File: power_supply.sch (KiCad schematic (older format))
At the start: 1 part

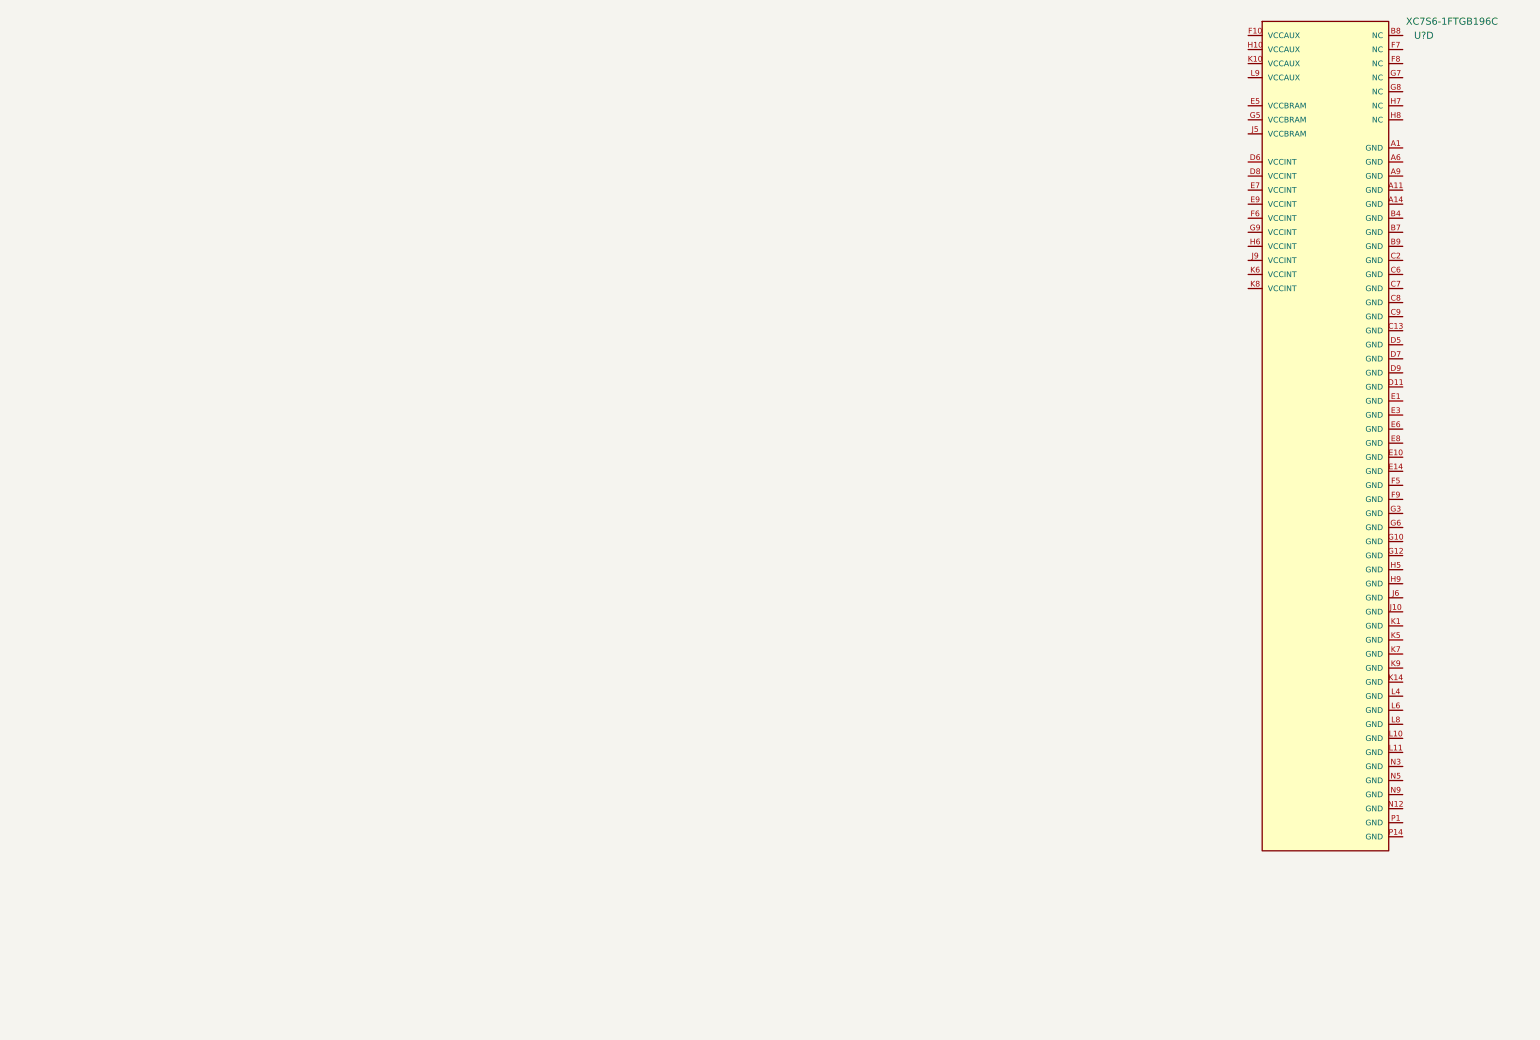
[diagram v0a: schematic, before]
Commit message: FPGA supply notes
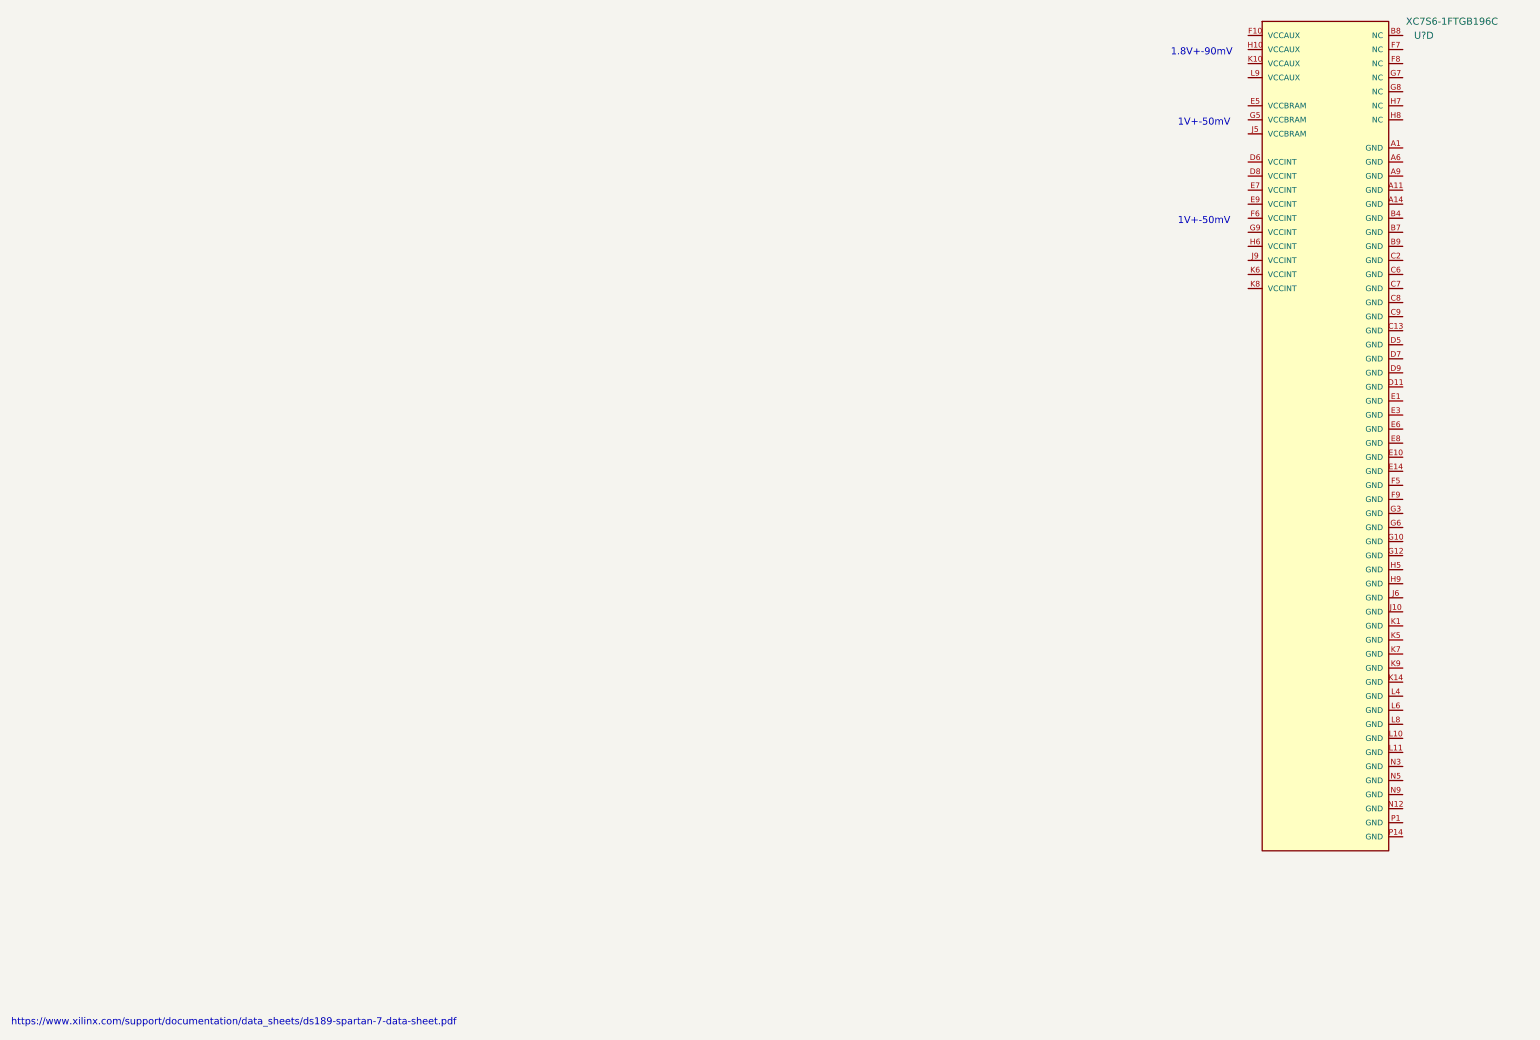
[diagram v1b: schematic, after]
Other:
- note added: "1.8V+-90mV"
- note added: "1V+-50mV"
- note added: "https://www.xilinx.com/support/documentation/data_sheets/ds189-spartan-7-data-sheet.pdf"
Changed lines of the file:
@@
 $Descr A4 11693 8268
 encoding utf-8
-Sheet 1 1
+Sheet 13 14
 Title "Open HF SDR FPGA Sheet"
 Date "2021-01-16"
@@
 	1    0    0    -1
 $EndComp
+Text Notes 8900 2000 0    50   ~ 0
+1V+-50mV
+Text Notes 600  7700 0    50   ~ 0
+https://www.xilinx.com/support/documentation/data_sheets/ds189-spartan-7-data-sheet.pdf
+Text Notes 8850 800  0    50   ~ 0
+1.8V+-90mV
+Text Notes 8900 1300 0    50   ~ 0
+1V+-50mV
 $EndSCHEMATC

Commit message: PSU init
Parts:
- added C? (x4): 4u7, symbol Device:C
- added C? (x2): 100n, symbol Device:C
- added L?: 47u, symbol Device:L
- added L?: 68u, symbol Device:L
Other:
- note added: "https://datasheet.lcsc.com/szlcsc/Silergy-Corp-SY8029AIC_C207636.pdf"
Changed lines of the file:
@@
 Text Notes 8900 1300 0    50   ~ 0
 1V+-50mV
+Text Notes 2550 5250 0    50   ~ 0
+https://datasheet.lcsc.com/szlcsc/Silergy-Corp-SY8029AIC_C207636.pdf
+$Comp
+L Device:L L?
+U 1 1 600CB20B
+P 5150 2000
+F 0 "L?" V 4878 2000 50  0000 C CNN
+F 1 "47u" V 4969 2000 50  0000 C CNN
+F 2 "" H 5150 2000 50  0001 C CNN
+F 3 "~" H 5150 2000 50  0001 C CNN
+F 4 "93-01-06" V 5060 2000 50  0000 C CNN "Lomex"
+	1    5150 2000
+	0    1    1    0
+$EndComp
+$Comp
+L Device:C C?
+U 1 1 600CC1A7
+P 5450 2200
+F 0 "C?" H 5565 2291 50  0000 L CNN
+F 1 "4u7" H 5565 2200 50  0000 L CNN
+F 2 "" H 5488 2050 50  0001 C CNN
+F 3 "~" H 5450 2200 50  0001 C CNN
+F 4 "82-06-22" H 5565 2109 50  0000 L CNN "Lomex"
+	1    5450 2200
+	1    0    0    -1
+$EndComp
+$Comp
+L Device:C C?
+U 1 1 600CC714
+P 6100 2200
+F 0 "C?" H 6215 2291 50  0000 L CNN
+F 1 "4u7" H 6215 2200 50  0000 L CNN
+F 2 "" H 6138 2050 50  0001 C CNN
+F 3 "~" H 6100 2200 50  0001 C CNN
+F 4 "82-06-22" H 6215 2109 50  0000 L CNN "Lomex"
+	1    6100 2200
+	1    0    0    -1
+$EndComp
+$Comp
+L Device:C C?
+U 1 1 600CD1F2
+P 6750 2200
+F 0 "C?" H 6865 2246 50  0000 L CNN
+F 1 "100n" H 6865 2155 50  0000 L CNN
+F 2 "" H 6788 2050 50  0001 C CNN
+F 3 "~" H 6750 2200 50  0001 C CNN
+	1    6750 2200
+	1    0    0    -1
+$EndComp
+$Comp
+L Device:L L?
+U 1 1 600D147C
+P 5150 900
+F 0 "L?" V 4878 900 50  0000 C CNN
+F 1 "68u" V 4969 900 50  0000 C CNN
+F 2 "" H 5150 900 50  0001 C CNN
+F 3 "~" H 5150 900 50  0001 C CNN
+F 4 " 93-03-36" V 5060 900 50  0000 C CNN "Lomex"
+	1    5150 900
+	0    1    1    0
+$EndComp
+$Comp
+L Device:C C?
+U 1 1 600D2019
+P 5450 1150
+F 0 "C?" H 5565 1241 50  0000 L CNN
+F 1 "4u7" H 5565 1150 50  0000 L CNN
+F 2 "" H 5488 1000 50  0001 C CNN
+F 3 "~" H 5450 1150 50  0001 C CNN
+F 4 "82-06-22" H 5565 1059 50  0000 L CNN "Lomex"
+	1    5450 1150
+	1    0    0    -1
+$EndComp
+$Comp
+L Device:C C?
+U 1 1 600D222E
+P 6100 1150
+F 0 "C?" H 6215 1241 50  0000 L CNN
+F 1 "4u7" H 6215 1150 50  0000 L CNN
+F 2 "" H 6138 1000 50  0001 C CNN
+F 3 "~" H 6100 1150 50  0001 C CNN
+F 4 "82-06-22" H 6215 1059 50  0000 L CNN "Lomex"
+	1    6100 1150
+	1    0    0    -1
+$EndComp
+$Comp
+L Device:C C?
+U 1 1 600D2238
+P 6750 1150
+F 0 "C?" H 6865 1196 50  0000 L CNN
+F 1 "100n" H 6865 1105 50  0000 L CNN
+F 2 "" H 6788 1000 50  0001 C CNN
+F 3 "~" H 6750 1150 50  0001 C CNN
+	1    6750 1150
+	1    0    0    -1
+$EndComp
 $EndSCHEMATC

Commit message: Power supplies
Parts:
- removed C? (x2): 4u7, symbol Device:C
- removed C?: 100n, symbol Device:C
- added C? (x24): C, symbol Device:C
- added C? (x4): 4u7, symbol Device:C
- added C? (x2): 100n, symbol Device:C
- added L?: L, symbol Device:L
- added R? (x7): R, symbol Device:R
- added U? (x6): SY8029, Package_TO_SOT_SMD:TSOT-23-8_HandSoldering, symbol sdr:SY8029
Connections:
- net at U?.D6 (VCCINT): now also L?.1, U?.D8 (VCCINT), U?.E5 (VCCBRAM), U?.E7 (VCCINT), U?.E9 (VCCINT), U?.F6 (VCCINT), U?.G5 (VCCBRAM), U?.G9 (VCCINT), U?.H6 (VCCINT), U?.J5 (VCCBRAM), U?.J9 (VCCINT), U?.K6 (VCCINT), U?.K8 (VCCINT), C?.1, C?.1, C?.1, C?.1, C?.1, C?.1, C?.1, C?.1, C?.1, C?.1, C?.1, R?.1
- net at U?.F10 (VCCAUX): now also C?.1, C?.1, C?.1, L?.1, U?.H10 (VCCAUX), U?.K10 (VCCAUX), U?.L9 (VCCAUX), C?.1, C?.1, C?.1, C?.1, C?.1, C?.1, C?.1, C?.1, R?.1
- net at L?.2: now also U?.5 (OUT)
- net at L?.2: now also U?.3 (OUT)
- net GNDD: now reaches C?.2
- net GNDD: now also C?.2, C?.2, C?.2, C?.2, C?.2, C?.2, C?.2, C?.2, R?.2, R?.2, R?.2, R?.2, U?.4 (GND), U?.8 (FB)
- new net: R?.1, R?.2, U?.1 (FB) (x2)
- new net: R?.1, R?.1, R?.2, U?.8 (FB)
- new net: C?.1, C?.1, C?.1, C?.1, C?.1, C?.1, C?.1, C?.1, C?.1, C?.1, C?.1, L?.1, R?.1
- new net: L?.2, U?.3 (OUT)
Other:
- note added: "3.3V"
- note added: "Filter at FPGA"
- note added: "Filter at SMPS"
- note removed: "https://datasheet.lcsc.com/szlcsc/Silergy-Corp-SY8029AIC_C207636.pdf"
- moved on the sheet: C?, L?

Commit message: finish up power supply
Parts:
- removed C? (x2): 4u7, symbol Device:C
- removed C?: 100n, symbol Device:C
- removed C? (x8): C, symbol Device:C
- removed L?: L, symbol Device:L
- removed R? (x2): R, symbol Device:R
- removed U? (x3): SY8029, Package_TO_SOT_SMD:TSOT-23-8_HandSoldering, symbol sdr:SY8029
- added C? (x2): 100n, symbol Device:C
- added C? (x5): 10n, symbol Device:C
- added C? (x2): 47p, symbol Device:C
- added C? (x2): 1n, symbol Device:C
- added C? (x4): 47uF, symbol Device:C
- added C? (x2): 47u, symbol Device:C
- added D? (x2): BAT54CLT1G, symbol Device:D_Schottky
- added D?: ZMM3V3, symbol Device:D_Zener
- added D? (x2): LED, symbol Device:LED
- added J?: Barrel_Jack, symbol Connector:Barrel_Jack
- added J?: _BAT_PROT, symbol Connector:Conn_01x02_Male
- added L?: 6.8u, symbol Device:L
- added L?: 330u, symbol Device:L
- added R? (x4): 10k, symbol Device:R
- added R?: 3.24k, symbol Device:R
- added R?: 1.7k, symbol Device:R
- added R?: 0, symbol Device:R
- added R?: 8k, symbol Device:R
- added R? (x2): 1k, symbol Device:R
- added R?: 470, symbol Device:R
- added U? (x2): TPS54331, symbol sdr:TPS54331
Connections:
- net labels added: +3V3, +5VA, GNDA, PWR_EN, VIN
- wire segments 85 -> 130
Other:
- note added: "10mV ripple with 0.1 ohm ESR per cap"
- note added: "40mVpp ripple with 0.1 ohm ESR per cap"
- note added: "Battery protection"
- note added: "Farnell 2725244"
- note added: "If the jumper is off, and VIN goes below 11.25V, PWR_EN \nwill go below 1.25V, switching off the power.\nThis avoids deep cycling lead acid batteries"
- note added: "Input decoupling\n"
- note added: "Lomex: 55-01-84"
- note added: "Power requirements\n1.8V 1A FPGA\n1V 1A FPGA\n3V3 1.5A FPGA + 1.2A for 1V and 1.8V buck inputs\n5V5 0.1A receiver"
- note removed: "3.3V"
- moved on the sheet: U?D

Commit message: update buck converter diodes
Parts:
- D? (x2): value BAT54CLT1G -> SS34
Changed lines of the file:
@@
 P 6050 3700
 F 0 "D?" V 6150 3550 50  0000 L CNN
-F 1 "BAT54CLT1G" V 6250 3450 50  0000 L CNN
+F 1 "SS34" V 6250 3450 50  0000 L CNN
 F 2 "" H 6050 3700 50  0001 C CNN
 F 3 "~" H 6050 3700 50  0001 C CNN
@@
 P 6000 5450
 F 0 "D?" V 6100 5300 50  0000 L CNN
-F 1 "BAT54CLT1G" V 6200 5200 50  0000 L CNN
+F 1 "SS34" V 6200 5200 50  0000 L CNN
 F 2 "" H 6000 5450 50  0001 C CNN
 F 3 "~" H 6000 5450 50  0001 C CNN

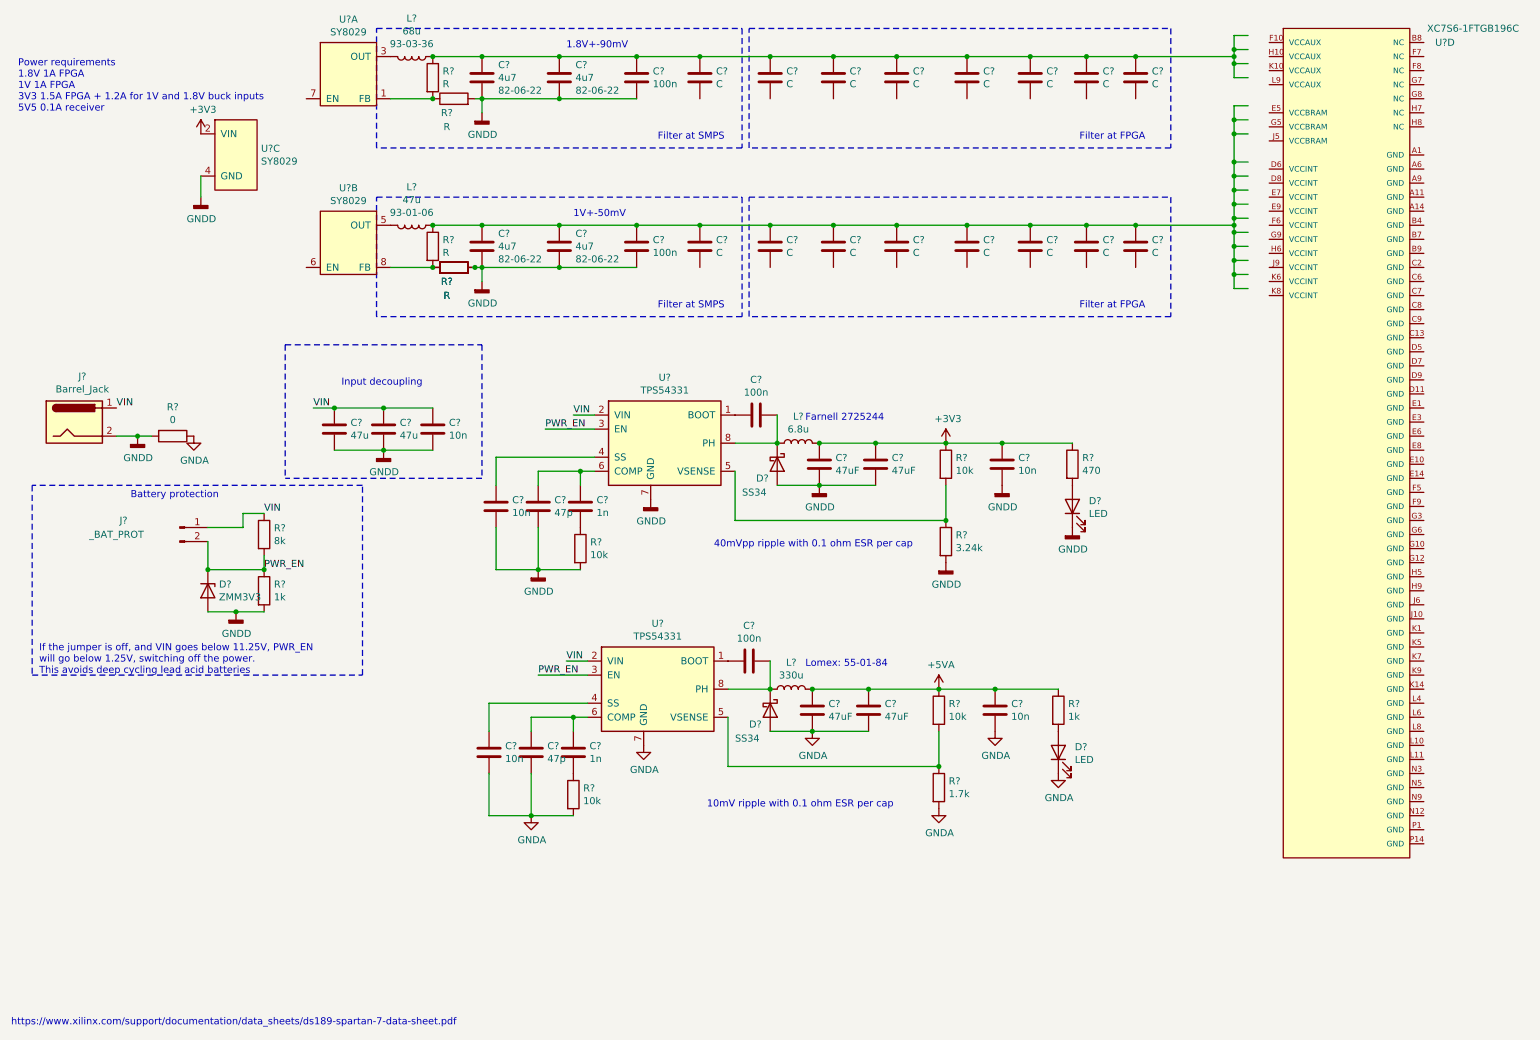
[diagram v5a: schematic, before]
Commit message: add power on sequencing for fpga
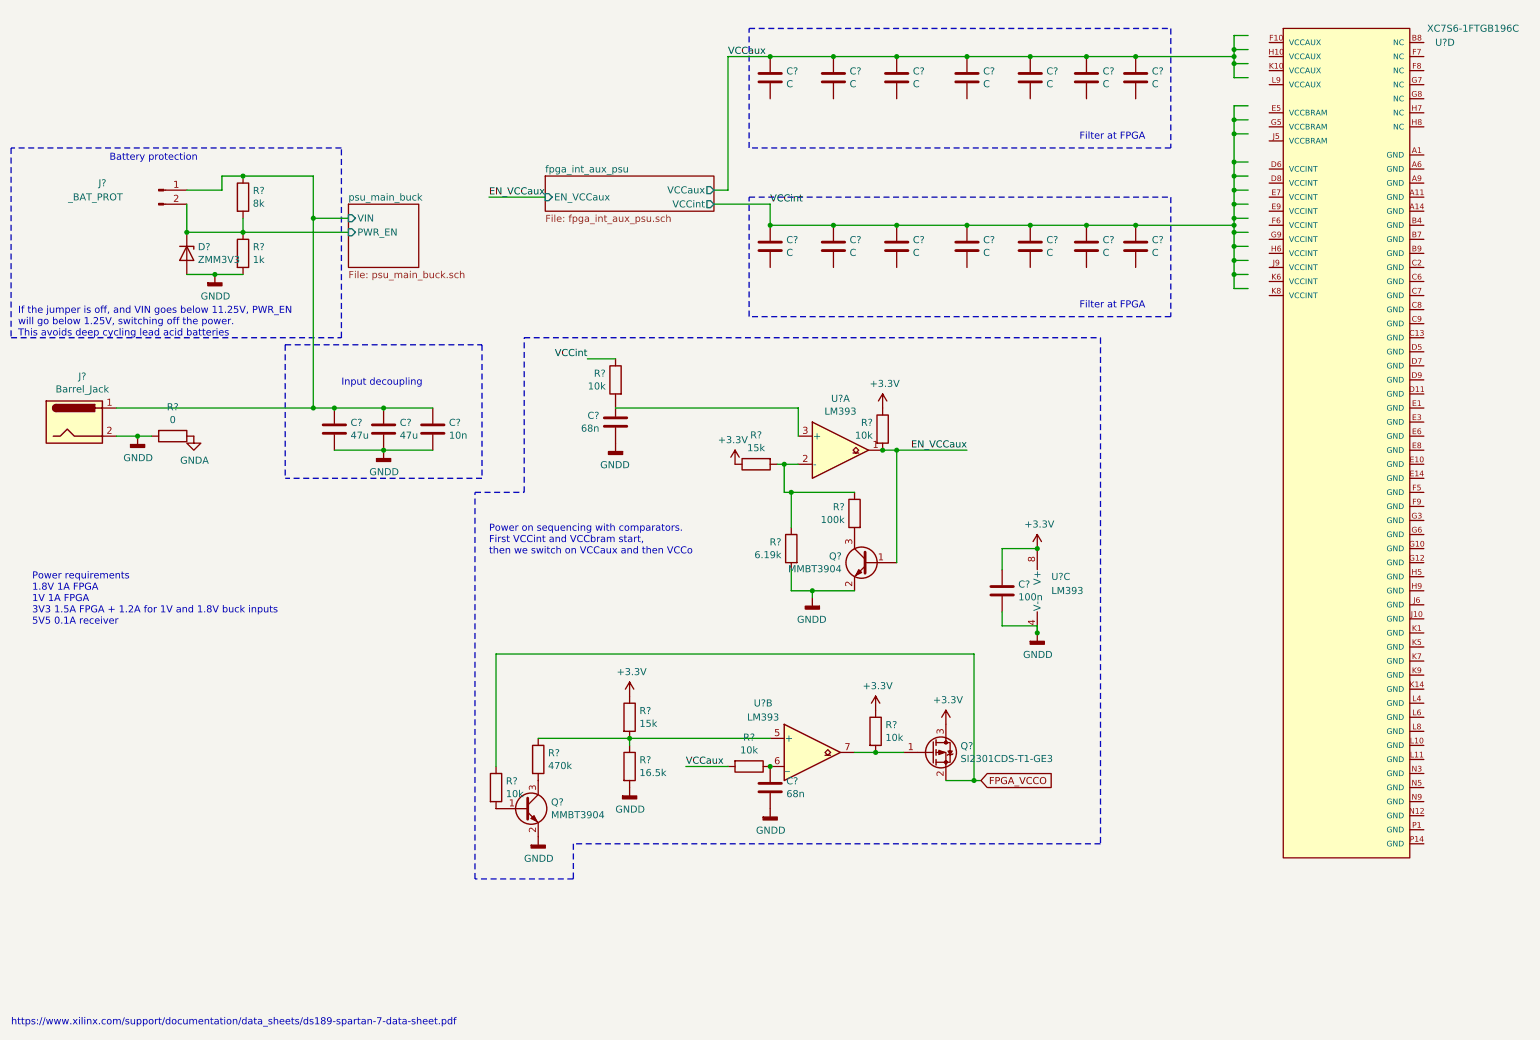
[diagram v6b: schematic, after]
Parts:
- removed C? (x4): 4u7, symbol Device:C
- removed C? (x4): 100n, symbol Device:C
- removed C? (x2): C, symbol Device:C
- removed C? (x4): 10n, symbol Device:C
- removed C? (x2): 47p, symbol Device:C
- removed C? (x2): 1n, symbol Device:C
- removed C? (x4): 47uF, symbol Device:C
- removed D? (x2): SS34, symbol Device:D_Schottky
- removed D? (x2): LED, symbol Device:LED
- removed L?: 47u, symbol Device:L
- removed L?: 68u, symbol Device:L
- removed L?: 6.8u, symbol Device:L
- removed L?: 330u, symbol Device:L
- removed R? (x5): R, symbol Device:R
- removed R? (x4): 10k, symbol Device:R
- removed R?: 3.24k, symbol Device:R
- removed R?: 1.7k, symbol Device:R
- removed R?: 470, symbol Device:R
- removed R?: 1k, symbol Device:R
- removed U? (x3): SY8029, Package_TO_SOT_SMD:TSOT-23-8_HandSoldering, symbol sdr:SY8029
- removed U? (x2): TPS54331, symbol sdr:TPS54331
- added C? (x2): 68n, symbol Device:C
- added C?: 100n, symbol Device:C
- added Q? (x2): MMBT3904, symbol Device:Q_NPN_BEC
- added Q?: SI2301CDS-T1-GE3, symbol Device:Q_PMOS_GSD
- added R? (x5): 10k, symbol Device:R
- added R? (x2): 15k, symbol Device:R
- added R?: 6.19k, symbol Device:R
- added R?: 100k, symbol Device:R
- added R?: 16.5k, symbol Device:R
- added R?: 470k, symbol Device:R
- added U? (x3): LM393, symbol Comparator:LM393
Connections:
- net labels added: +3.3V, EN_VCCaux, FPGA_VCCO, VCCaux, VCCint
- net labels removed: +3V3, +5VA, PWR_EN, VIN
- wire segments 130 -> 107
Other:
- note added: "Power on sequencing with comparators. \nFirst VCCint and VCCbram start, \nthen we switch on VCCaux and then VCCo\n"
- note removed: "1.8V+-90mV"
- note removed: "10mV ripple with 0.1 ohm ESR per cap"
- note removed: "1V+-50mV"
- note removed: "40mVpp ripple with 0.1 ohm ESR per cap"
- note removed: "Farnell 2725244"
- note removed: "Filter at SMPS"
- note removed: "Lomex: 55-01-84"
- moved on the sheet: D?, J?, R?
